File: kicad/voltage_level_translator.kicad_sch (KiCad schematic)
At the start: 15 parts, among them Q1 2N7002, U3 TMUX1574PW, U7 TMUX1574PW, U8 TXS0108EPW, U9 TXS0108EPW

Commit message: Updated wiring
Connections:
- net IO18_H: now also U8.16 (B4)
- net IO18_L: now also U9.5 (A4)
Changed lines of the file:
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@@
+	(wire
+		(pts
+			(xy 36.83 127) (xy 41.91 127)
+		)
+		(stroke
+			(width 0)
+			(type default)
+		)
+	)
 	(wire
 		(pts
@@
 		(pts
 			(xy 231.14 30.48) (xy 232.41 30.48)
-		)
-		(stroke
-			(width 0)
-			(type default)
-		)
-	)
-	(wire
-		(pts
-			(xy 36.83 127) (xy 41.91 127)
 		)
 		(stroke
@@
 		)
 	)
-	(label "IO18_L"
-		(at 36.8095 127 180)
-		(effects
-			(font
-				(size 1.27 1.27)
-			)
-			(justify right bottom)
-		)
-	)
 	(label "IO13_H"
 		(at 266.7 135.89 0)
@@
 		)
 	)
+	(label "IO18_H"
+		(at 69.85 50.8 0)
+		(effects
+			(font
+				(size 1.27 1.27)
+			)
+			(justify left bottom)
+		)
+	)
 	(label "D1_K"
 		(at 140.97 74.93 0)
@@
 		)
 	)
-	(label "IO18_H"
-		(at 69.8705 50.8 0)
-		(effects
-			(font
-				(size 1.27 1.27)
-			)
-			(justify left bottom)
-		)
-	)
 	(label "IO11_H"
 		(at 69.85 55.88 0)
@@
 		)
 	)
+	(label "IO18_L"
+		(at 36.83 127 180)
+		(effects
+			(font
+				(size 1.27 1.27)
+			)
+			(justify right bottom)
+		)
+	)

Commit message: Partial re-wiring
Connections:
- net +3.3V: now also U8.10 (OE), U9.10 (OE)
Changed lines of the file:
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@@
+	(wire
+		(pts
+			(xy 39.37 116.84) (xy 41.91 116.84)
+		)
+		(stroke
+			(width 0)
+			(type default)
+		)
+	)
 	(wire
 		(pts
@@
 	(wire
 		(pts
+			(xy 39.37 114.935) (xy 39.37 116.84)
+		)
+		(stroke
+			(width 0)
+			(type default)
+		)
+	)
+	(wire
+		(pts
 			(xy 160.02 74.93) (xy 165.1 74.93)
 		)
@@
 	(wire
 		(pts
+			(xy 43.815 40.64) (xy 45.72 40.64)
+		)
+		(stroke
+			(width 0)
+			(type default)
+		)
+	)
+	(wire
+		(pts
 			(xy 234.95 120.65) (xy 236.22 120.65)
 		)
@@
 		(pts
 			(xy 240.03 100.33) (xy 248.92 100.33)
+		)
+		(stroke
+			(width 0)
+			(type default)
+		)
+	)
+	(wire
+		(pts
+			(xy 43.815 38.735) (xy 43.815 40.64)
 		)
 		(stroke
@@
 		)
 	)
-	(label "N-GATE"
+	(label "GATE"
 		(at 157.48 74.93 0)
 		(effects
@@
 				(path "/07b4bde2-66d8-4845-8f7d-da280a4d29f6/4e83f8d5-a547-42b8-8426-b71a9f8b331b"
 					(reference "#PWR048")
+					(unit 1)
+				)
+			)
+		)
+	)
+	(symbol
+		(lib_id "power:+3.3V")
+		(at 43.815 38.735 0)
+		(unit 1)
+		(exclude_from_sim no)
+		(in_bom yes)
+		(on_board yes)
+		(dnp no)
+		(fields_autoplaced yes)
+		(property "Reference" "#PWR023"
+			(at 43.815 42.545 0)
+			(effects
+				(font
+					(size 1.27 1.27)
+				)
+				(hide yes)
+			)
+		)
+		(property "Value" "+3.3V"
+			(at 43.815 34.29 0)
+			(effects
+				(font
+					(size 1.27 1.27)
+				)
+			)
+		)
+		(property "Footprint" ""
+			(at 43.815 38.735 0)
+			(effects
+				(font
+					(size 1.27 1.27)
+				)
+				(hide yes)
+			)
+		)
+		(property "Datasheet" ""
+			(at 43.815 38.735 0)
+			(effects
+				(font
+					(size 1.27 1.27)
+				)
+				(hide yes)
+			)
+		)
+		(property "Description" "Power symbol creates a global label with name \"+3.3V\""
+			(at 43.815 38.735 0)
+			(effects
+				(font
+					(size 1.27 1.27)
+				)
+				(hide yes)
+			)
+		)
+		(pin "1"
+		)
+		(instances
+			(project "ESP32-Bus-Pirate-Dock"
+				(path "/07b4bde2-66d8-4845-8f7d-da280a4d29f6/4e83f8d5-a547-42b8-8426-b71a9f8b331b"
+					(reference "#PWR023")
 					(unit 1)
 				)
@@
 					(unit 1)
 				)
+			)
+		)
+	)
+	(symbol
+		(lib_id "power:+3.3V")
+		(at 39.37 114.935 0)
+		(unit 1)
+		(exclude_from_sim no)
+		(in_bom yes)
+		(on_board yes)
+		(dnp no)
+		(fields_autoplaced yes)
+		(property "Reference" "#PWR012"
+			(at 39.37 118.745 0)
+			(effects
+				(font
+					(size 1.27 1.27)
+				)
+				(hide yes)
+			)
+		)
+		(property "Value" "+3.3V"
+			(at 39.37 110.49 0)
+			(effects
+				(font
+					(size 1.27 1.27)
+				)
+			)
+		)
+		(property "Footprint" ""
+			(at 39.37 114.935 0)
+			(effects
+				(font
+					(size 1.27 1.27)
+				)
+				(hide yes)
+			)
+		)
+		(property "Datasheet" ""
+			(at 39.37 114.935 0)
+			(effects
+				(font
+					(size 1.27 1.27)
+				)
+				(hide yes)
+			)
+		)
+		(property "Description" "Power symbol creates a global label with name \"+3.3V\""
+			(at 39.37 114.935 0)
+			(effects
+				(font
+					(size 1.27 1.27)
+				)
+				(hide yes)
+			)
+		)
+		(pin "1"
+		)
+		(instances
+			(project "ESP32-Bus-Pirate-Dock"
+				(path "/07b4bde2-66d8-4845-8f7d-da280a4d29f6/4e83f8d5-a547-42b8-8426-b71a9f8b331b"
+					(reference "#PWR012")
+					(unit 1)
+				)

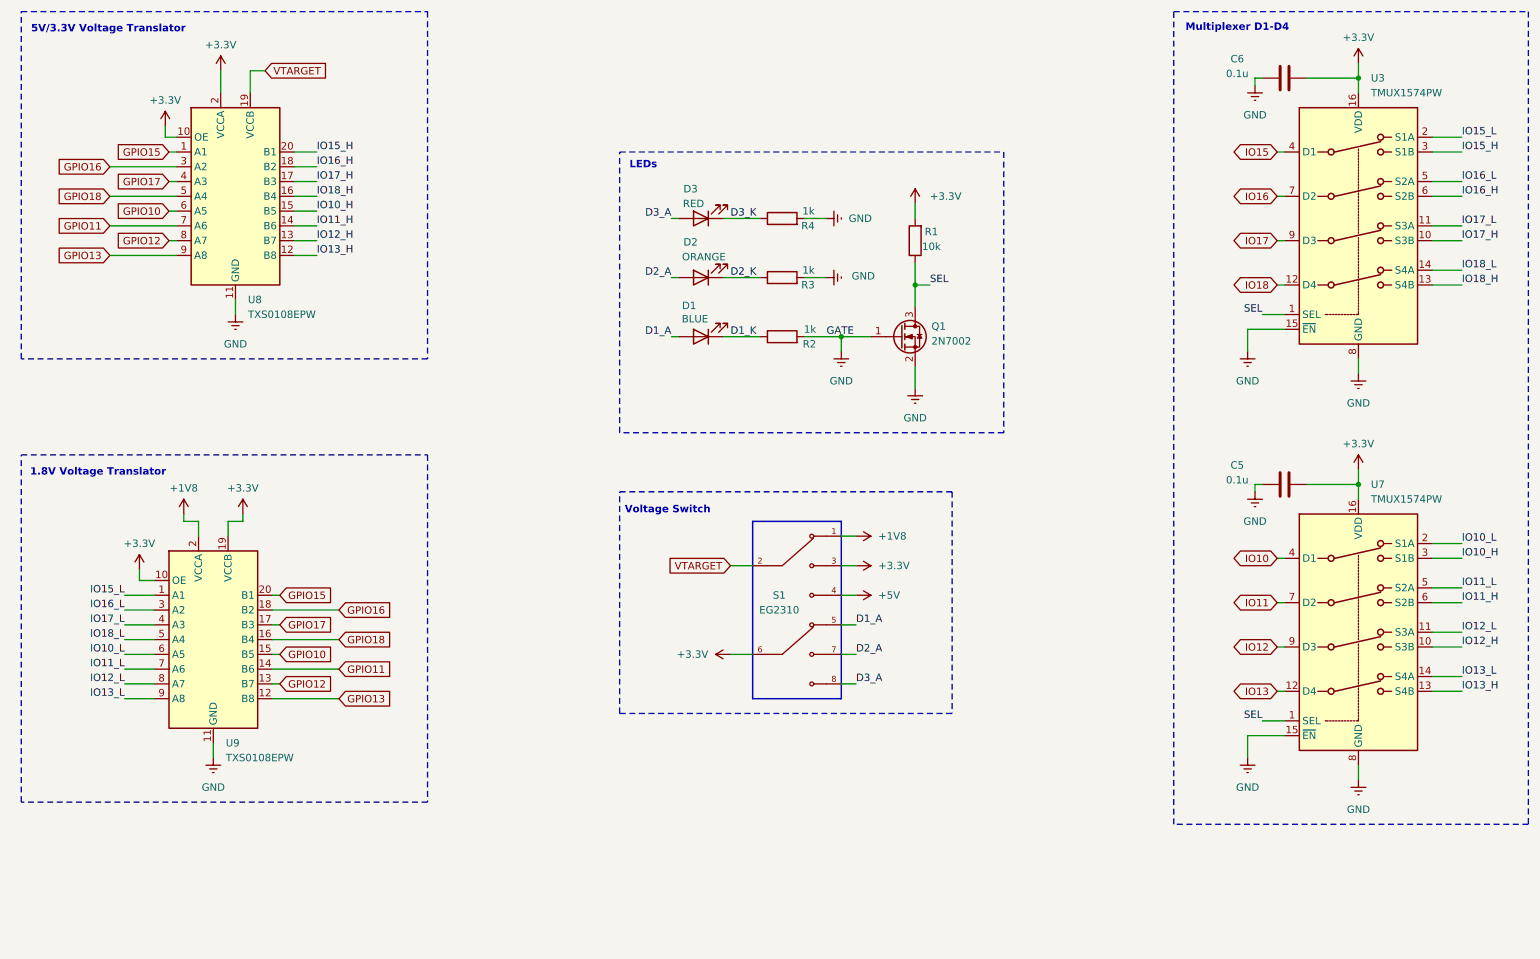
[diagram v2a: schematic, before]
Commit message: Updated enable logic for translators
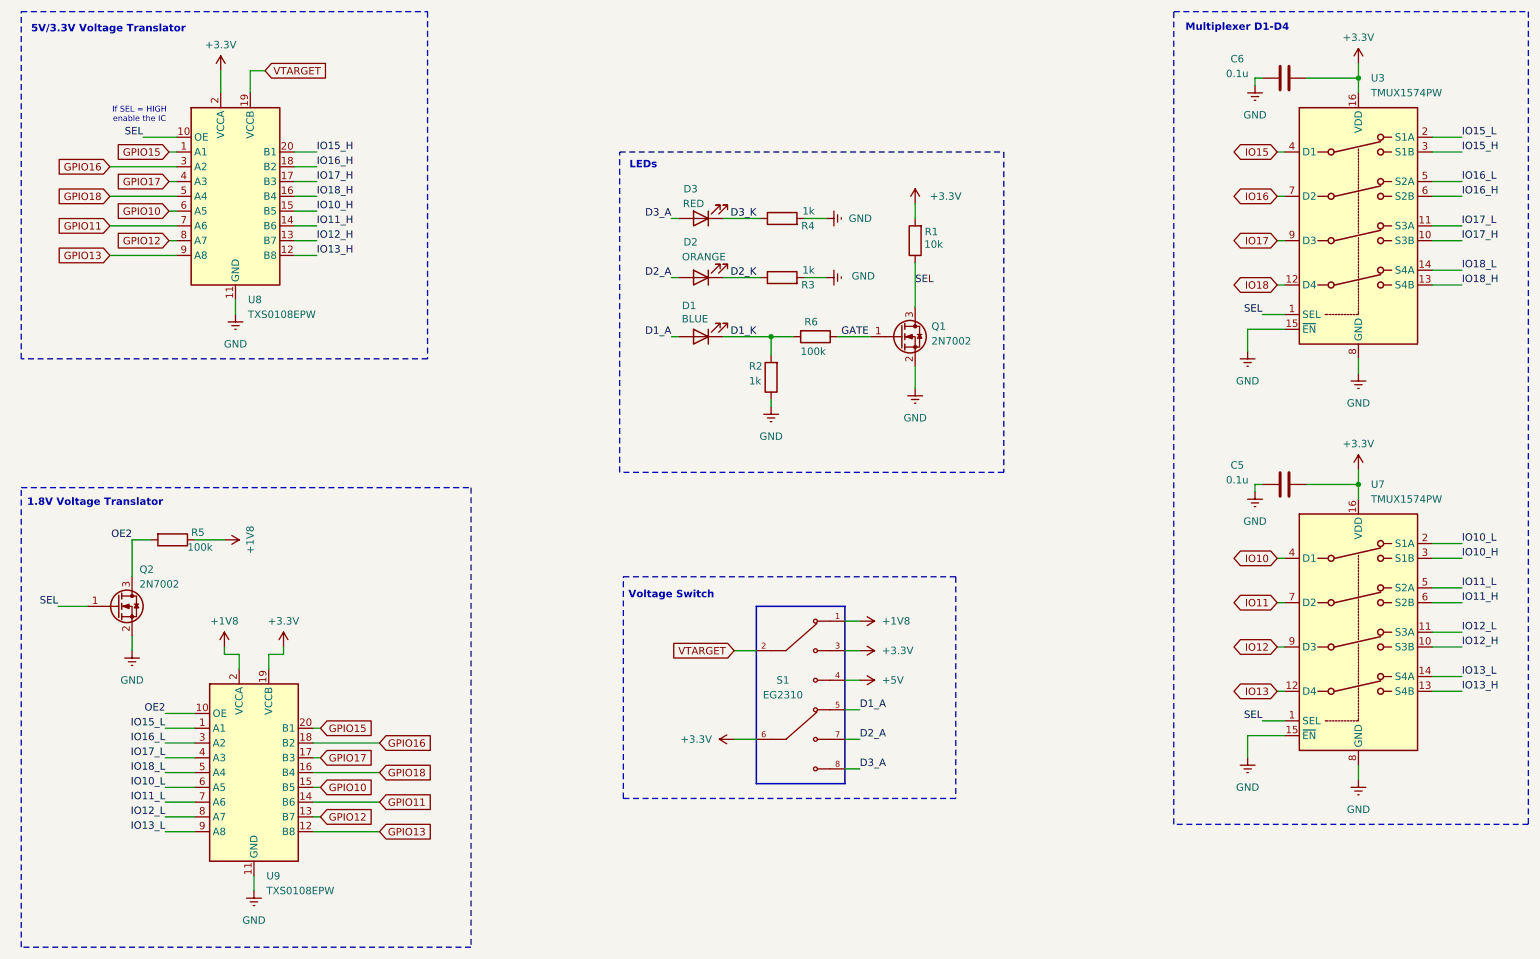
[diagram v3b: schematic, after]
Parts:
- added Q2: 2N7002, Package_TO_SOT_SMD:SOT-23, symbol Transistor_FET:2N7002
- added R5, R6: 100k, Resistor_SMD:R_0805_2012Metric, symbol Device:R
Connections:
- net +1V8: now also R5.1
- net +3.3V: no longer U8.10 (OE), U9.10 (OE)
- net D1_K: now also R2.2, R6.2; no longer R2.1
- net GND: now also R2.1, Q2.2 (S); no longer Q1.1 (G), R2.2
- net SEL: now also U8.10 (OE), Q2.1 (G)
- new net GATE: Q1.1 (G), R6.1
- new net OE2: Q2.3 (D), R5.2, U9.10 (OE)
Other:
- note added: "If SEL = HIGH enable the IC"
- moved on the sheet: R2, S1, U9

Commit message: Relabeled components
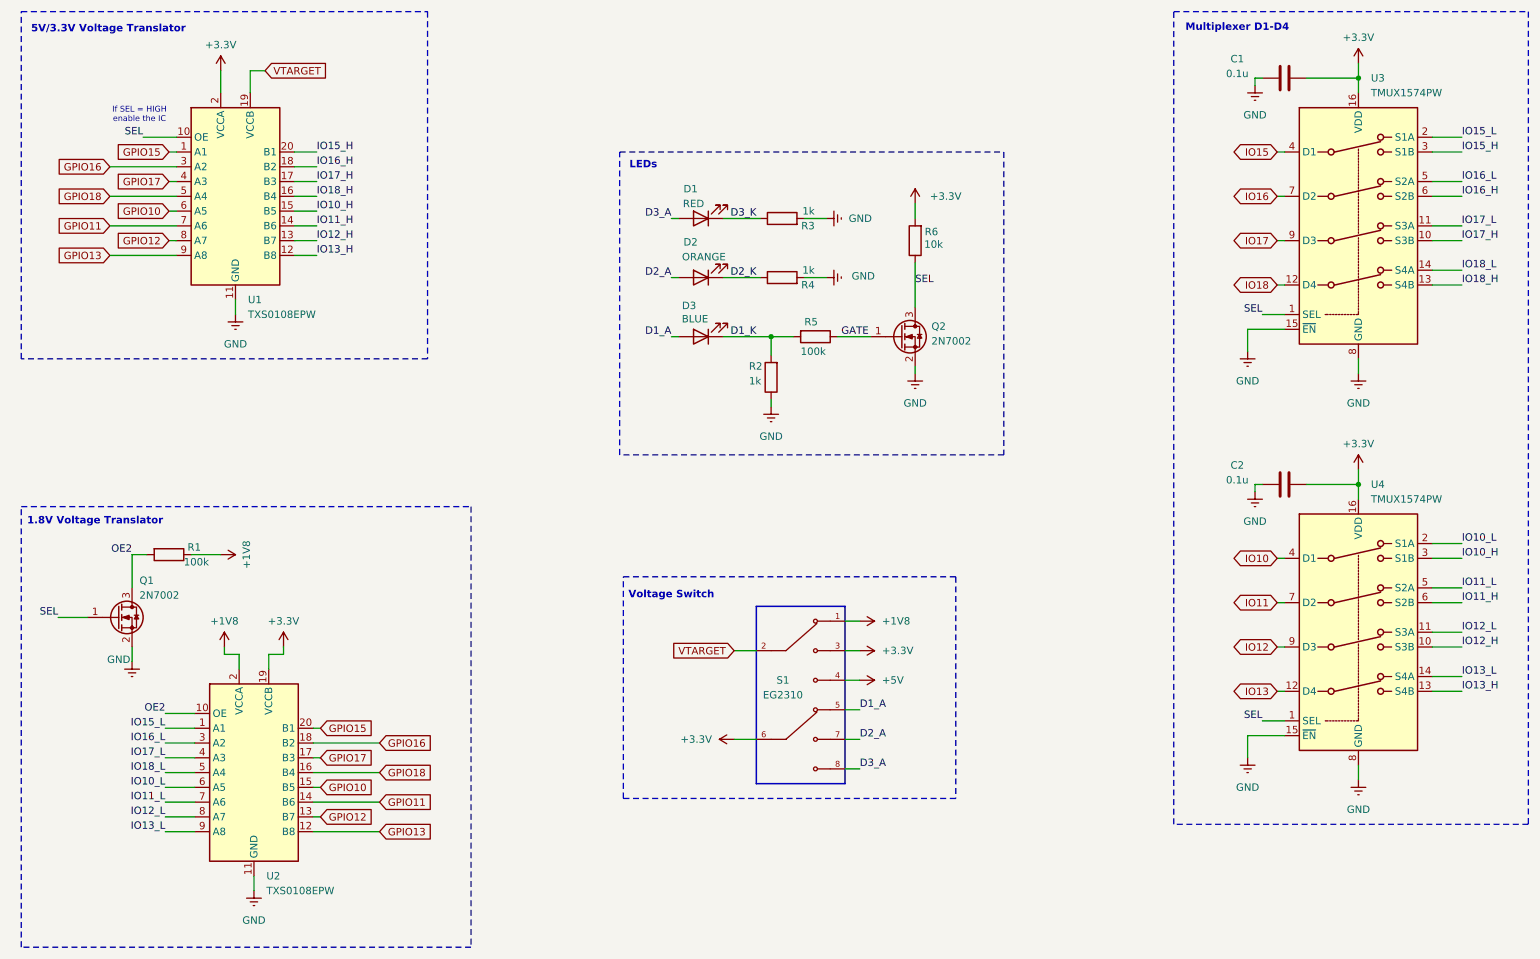
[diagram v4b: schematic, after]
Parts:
- renumbered C6 to C1, C5 to C2, D3 to D1, D1 to D3, Q2 to Q1, Q1 to Q2, R5 to R1, R4 to R3, R3 to R4, R6 to R5, R1 to R6, U8 to U1, U9 to U2, U7 to U4
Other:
- moved on the sheet: Q1, R1
